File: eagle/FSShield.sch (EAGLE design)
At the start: 37 parts, among them J1 057-040-1, J2 057-040-1, U1 LM7322QMAX/NOPB, X1 C-GRID-03-70543

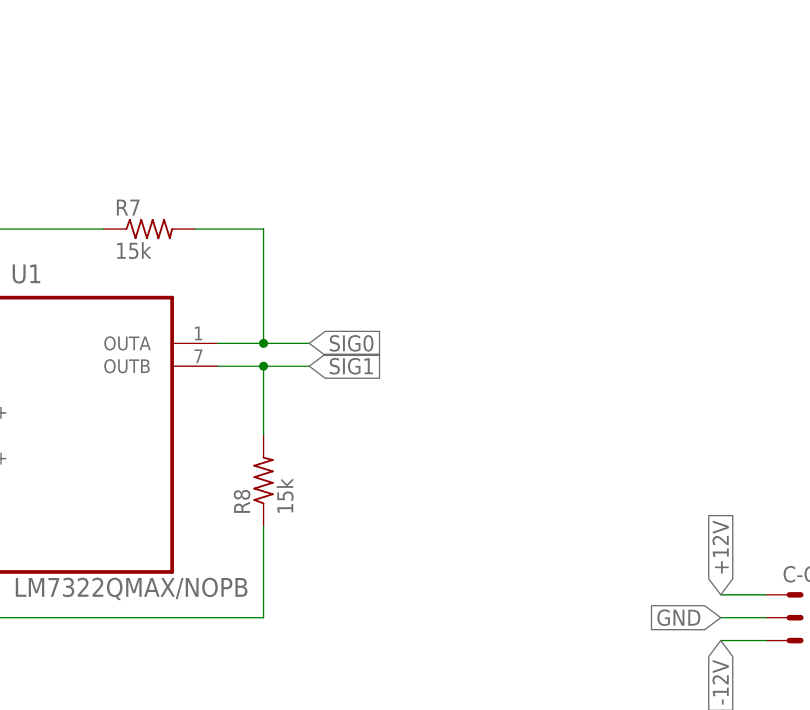
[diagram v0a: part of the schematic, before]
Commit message: removed DAC code. Updated eagle files.
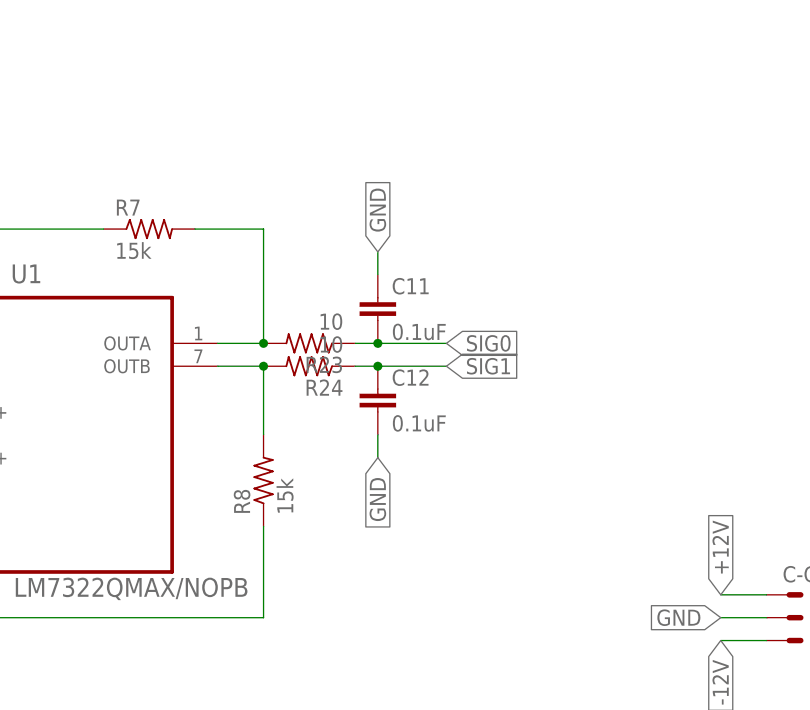
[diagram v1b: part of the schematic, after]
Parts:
- added C11, C12: 0.1uF, SparkFun-Capacitors:0.1UF-0603-25V-(+80/-20%)
- added R23, R24: 10, resistor:R-US_M0805
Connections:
- new net N$5: C12.1, R24.1
- new net N$6: C11.2, R23.1
- net GND: now also C11.1, C12.2
- net SIG0: now also R23.2
- net SIG1: now also R24.2
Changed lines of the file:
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@@
 <part name="C9" library="SparkFun-Capacitors" library_urn="urn:adsk.eagle:library:510" deviceset="10NF" device="-0603-50V-10%" package3d_urn="urn:adsk.eagle:package:37414/1" value="10nF"/>
 <part name="C10" library="SparkFun-Capacitors" library_urn="urn:adsk.eagle:library:510" deviceset="10NF" device="-0603-50V-10%" package3d_urn="urn:adsk.eagle:package:37414/1" value="10nF"/>
+<part name="R23" library="resistor" library_urn="urn:adsk.eagle:library:348" deviceset="R-US_" device="M0805" package3d_urn="urn:adsk.eagle:package:23556/2" value="10"/>
+<part name="R24" library="resistor" library_urn="urn:adsk.eagle:library:348" deviceset="R-US_" device="M0805" package3d_urn="urn:adsk.eagle:package:23556/2" value="10"/>
+<part name="C11" library="SparkFun-Capacitors" library_urn="urn:adsk.eagle:library:510" deviceset="0.1UF" device="-0603-25V-(+80/-20%)" package3d_urn="urn:adsk.eagle:package:37414/1" value="0.1uF"/>
+<part name="C12" library="SparkFun-Capacitors" library_urn="urn:adsk.eagle:library:510" deviceset="0.1UF" device="-0603-25V-(+80/-20%)" package3d_urn="urn:adsk.eagle:package:37414/1" value="0.1uF"/>
 </parts>
 <sheets>
@@
 <attribute name="NAME" x="186.436" y="85.979" size="1.778" layer="95" font="vector" rot="R180"/>
 <attribute name="VALUE" x="186.436" y="91.059" size="1.778" layer="96" font="vector" rot="R180"/>
+</instance>
+<instance part="R23" gate="G$1" x="233.68" y="111.76" smashed="yes" rot="R180">
+<attribute name="NAME" x="237.49" y="110.2614" size="1.778" layer="95" rot="R180"/>
+<attribute name="VALUE" x="237.49" y="115.062" size="1.778" layer="96" rot="R180"/>
+</instance>
+<instance part="R24" gate="G$1" x="233.68" y="109.22" smashed="yes" rot="R180">
+<attribute name="NAME" x="237.49" y="107.7214" size="1.778" layer="95" rot="R180"/>
+<attribute name="VALUE" x="237.49" y="112.522" size="1.778" layer="96" rot="R180"/>
+</instance>
+<instance part="C11" gate="G$1" x="241.3" y="114.3" smashed="yes">
+<attribute name="NAME" x="242.824" y="117.221" size="1.778" layer="95" font="vector"/>
+<attribute name="VALUE" x="242.824" y="112.141" size="1.778" layer="96" font="vector"/>
+</instance>
+<instance part="C12" gate="G$1" x="241.3" y="104.14" smashed="yes">
+<attribute name="NAME" x="242.824" y="107.061" size="1.778" layer="95" font="vector"/>
+<attribute name="VALUE" x="242.824" y="101.981" size="1.778" layer="96" font="vector"/>
 </instance>
 </instances>
@@
 <junction x="261.62" y="-55.88"/>
 </segment>
+<segment>
+<pinref part="C11" gate="G$1" pin="1"/>
+<wire x1="241.3" y1="119.38" x2="241.3" y2="121.92" width="0.1524" layer="91"/>
+<label x="241.3" y="121.92" size="1.778" layer="95" rot="R90" xref="yes"/>
+</segment>
+<segment>
+<pinref part="C12" gate="G$1" pin="2"/>
+<wire x1="241.3" y1="101.6" x2="241.3" y2="99.06" width="0.1524" layer="91"/>
+<label x="241.3" y="99.06" size="1.778" layer="95" rot="R270" xref="yes"/>
+</segment>
 </net>
 <net name="DI_TOP_A" class="0">
@@
 <pinref part="U1" gate="A" pin="OUTA"/>
 <wire x1="223.52" y1="111.76" x2="228.6" y2="111.76" width="0.1524" layer="91"/>
-<label x="233.68" y="111.76" size="1.778" layer="95" xref="yes"/>
-<wire x1="228.6" y1="111.76" x2="233.68" y2="111.76" width="0.1524" layer="91"/>
+<label x="248.92" y="111.76" size="1.778" layer="95" xref="yes"/>
 <wire x1="228.6" y1="111.76" x2="228.6" y2="124.46" width="0.1524" layer="91"/>
-<junction x="228.6" y="111.76"/>
 <wire x1="228.6" y1="124.46" x2="220.98" y2="124.46" width="0.1524" layer="91"/>
 <pinref part="R7" gate="G$1" pin="2"/>
+<pinref part="R23" gate="G$1" pin="2"/>
+<junction x="228.6" y="111.76"/>
 </segment>
 </net>
@@
 <pinref part="U1" gate="A" pin="OUTB"/>
 <wire x1="223.52" y1="109.22" x2="228.6" y2="109.22" width="0.1524" layer="91"/>
-<label x="233.68" y="109.22" size="1.778" layer="95" xref="yes"/>
-<wire x1="228.6" y1="109.22" x2="233.68" y2="109.22" width="0.1524" layer="91"/>
+<label x="248.92" y="109.22" size="1.778" layer="95" xref="yes"/>
 <wire x1="228.6" y1="109.22" x2="228.6" y2="101.6" width="0.1524" layer="91"/>
+<pinref part="R8" gate="G$1" pin="2"/>
+<pinref part="R24" gate="G$1" pin="2"/>
 <junction x="228.6" y="109.22"/>
-<pinref part="R8" gate="G$1" pin="2"/>
 </segment>
 </net>
@@
 </segment>
 </net>
+<net name="N$5" class="0">
+<segment>
+<pinref part="R24" gate="G$1" pin="1"/>
+<pinref part="C12" gate="G$1" pin="1"/>
+<wire x1="241.3" y1="109.22" x2="238.76" y2="109.22" width="0.1524" layer="91"/>
+<wire x1="248.92" y1="109.22" x2="241.3" y2="109.22" width="0.1524" layer="91"/>
+<junction x="241.3" y="109.22"/>
+</segment>
+</net>
+<net name="N$6" class="0">
+<segment>
+<pinref part="R23" gate="G$1" pin="1"/>
+<pinref part="C11" gate="G$1" pin="2"/>
+<wire x1="241.3" y1="111.76" x2="238.76" y2="111.76" width="0.1524" layer="91"/>
+<wire x1="248.92" y1="111.76" x2="241.3" y2="111.76" width="0.1524" layer="91"/>
+<junction x="241.3" y="111.76"/>
+</segment>
+</net>
